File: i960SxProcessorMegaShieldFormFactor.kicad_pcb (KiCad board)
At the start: 4 copper layers, 101.6 x 53.3 mm, 44 parts, among them P1 Power, P2 Data Lines Lower, P3 Data Lines Upper, P4 Address Lines, P5 PWM, P6 Serializable Pins, P7 1284p Direct Connection, U1 74HC245, U2 74HC245, U3 80960Sx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

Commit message: More fix up actions
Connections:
- net /DT\~R renamed /DT\~{R}
- net /Sheet62305775/~MR0 renamed /Sheet62305775/~{MR0}
- net /Sheet62305775/~MR1 renamed /Sheet62305775/~{MR1}
- net /W\~R~ renamed /W\~{R}
- net /~AS renamed /~{AS}
- net /~BE0 renamed /~{BE0}
- net /~BE1 renamed /~{BE1}
- net /~BLAST~\~FAIL~ renamed /~{BLAST}\~{FAIL}
- net /~DEN renamed /~{DEN}
- net /~INT0 renamed /~{INT0}
- net /~INT3 renamed /~{INT3}
- net /~LOCK renamed /~{LOCK}
- net /~READY renamed /~{READY}
- net /~READY960 renamed /~{READY960}
- net /~RESET960 renamed /~{RESET960}
- P1 pad 1: Net-(P1-Pad1) -> unconnected-(P1-Pad1)
- P1 pad 3: Net-(P1-Pad3) -> unconnected-(P1-Pad3)
- P1 pad 8: Net-(P1-Pad8) -> unconnected-(P1-Pad8)
- P5 pad 5: Net-(P5-Pad5) -> unconnected-(P5-Pad5)
- U3 pad 23: Net-(U3-Pad23) -> unconnected-(U3-Pad23)
- U3 pad 42: Net-(U3-Pad42) -> unconnected-(U3-Pad42)
- U3 pad 50: Net-(U3-Pad50) -> unconnected-(U3-Pad50)
- U3 pad 65: Net-(U3-Pad65) -> unconnected-(U3-Pad65)
- U3 pad 75: Net-(U3-Pad75) -> unconnected-(U3-Pad75)
- U7 pad 12: Net-(U7-Pad12) -> unconnected-(U7-Pad12)
- U7 pad 13: Net-(U7-Pad13) -> unconnected-(U7-Pad13)
- U7 pad 14: Net-(U7-Pad14) -> unconnected-(U7-Pad14)
- U7 pad 15: Net-(U7-Pad15) -> unconnected-(U7-Pad15)
- U7 pad 2: Net-(U7-Pad2) -> unconnected-(U7-Pad2)
- U7 pad 3: Net-(U7-Pad3) -> unconnected-(U7-Pad3)
- U7 pad 4: Net-(U7-Pad4) -> unconnected-(U7-Pad4)
- U7 pad 5: Net-(U7-Pad5) -> unconnected-(U7-Pad5)
- U7 pad 6: Net-(U7-Pad6) -> unconnected-(U7-Pad6)
- U7 pad 7: Net-(U7-Pad7) -> unconnected-(U7-Pad7)
- U9 pad 14: Net-(U9-Pad14) -> unconnected-(U9-Pad14)
- U9 pad 15: Net-(U9-Pad15) -> unconnected-(U9-Pad15)
- U9 pad 2: Net-(U9-Pad2) -> unconnected-(U9-Pad2)
- U9 pad 3: Net-(U9-Pad3) -> unconnected-(U9-Pad3)
- U9 pad 4: Net-(U9-Pad4) -> unconnected-(U9-Pad4)
- U9 pad 5: Net-(U9-Pad5) -> unconnected-(U9-Pad5)
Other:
- net class Default removed
- net class Min removed
- board text added: "CLK N\C FAIL GND N\C ~{RDY ALE }AS ~{LOCK }BLAST"
- board text added: "DT\~{R }DEN W\~{R}"
- board text added: "HOLD HLDA ~{INT3 INT2 INT1}"
- board text added: "~{INT0 }RESET960 CLK2 ~{BE0 }BE1 BA1 BA2 BA3"
- board text removed: "CLK N\C FAIL GND N\C ~RDY ALE ~AS ~LOCK ~BLAST"
- board text removed: "DT\~R ~DEN W\~R"
- board text removed: "HOLD HLDA ~INT3 INT2 INT1"
- board text removed: "~INT0 ~RESET960 CLK2 ~BE0 ~BE1 BA1 BA2 BA3"

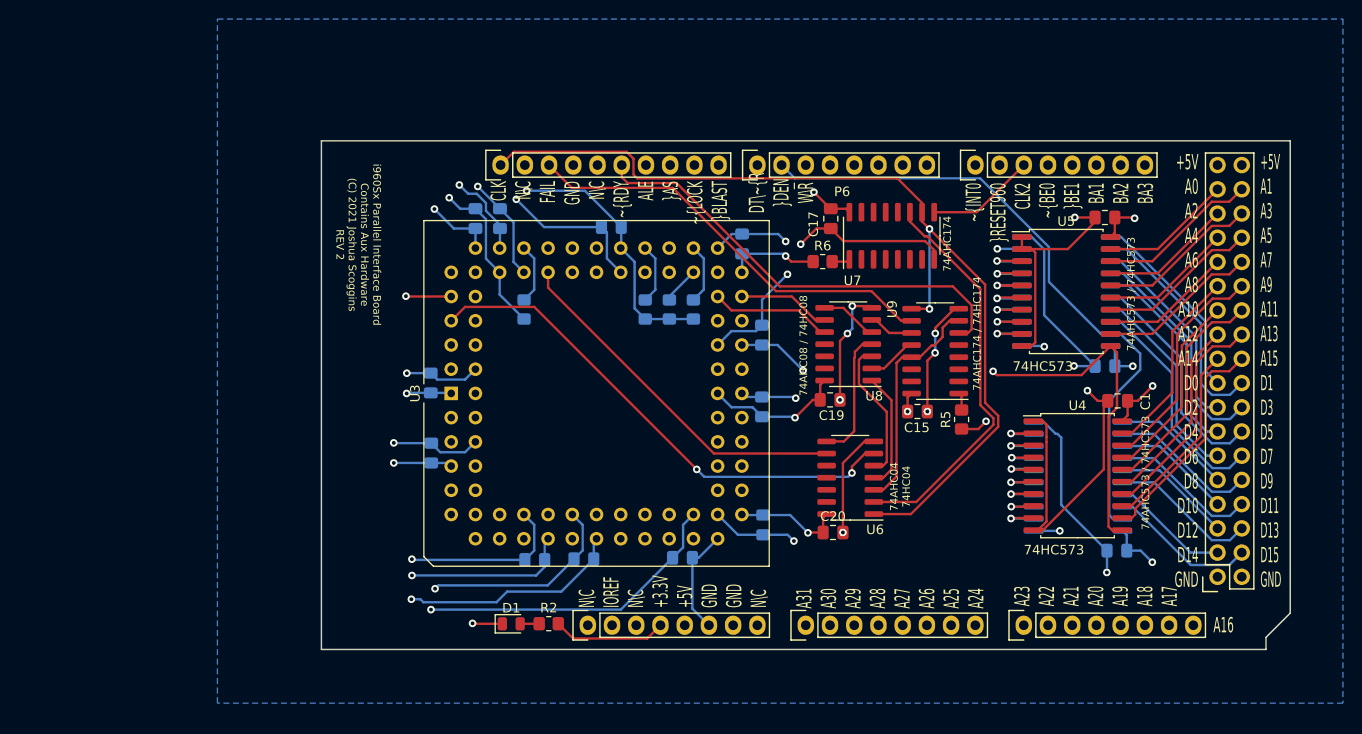
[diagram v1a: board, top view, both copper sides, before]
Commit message: Use a GAL chip to consolidate the number of chips
I have many extra free entries on the GAL to assist me in doing stuff
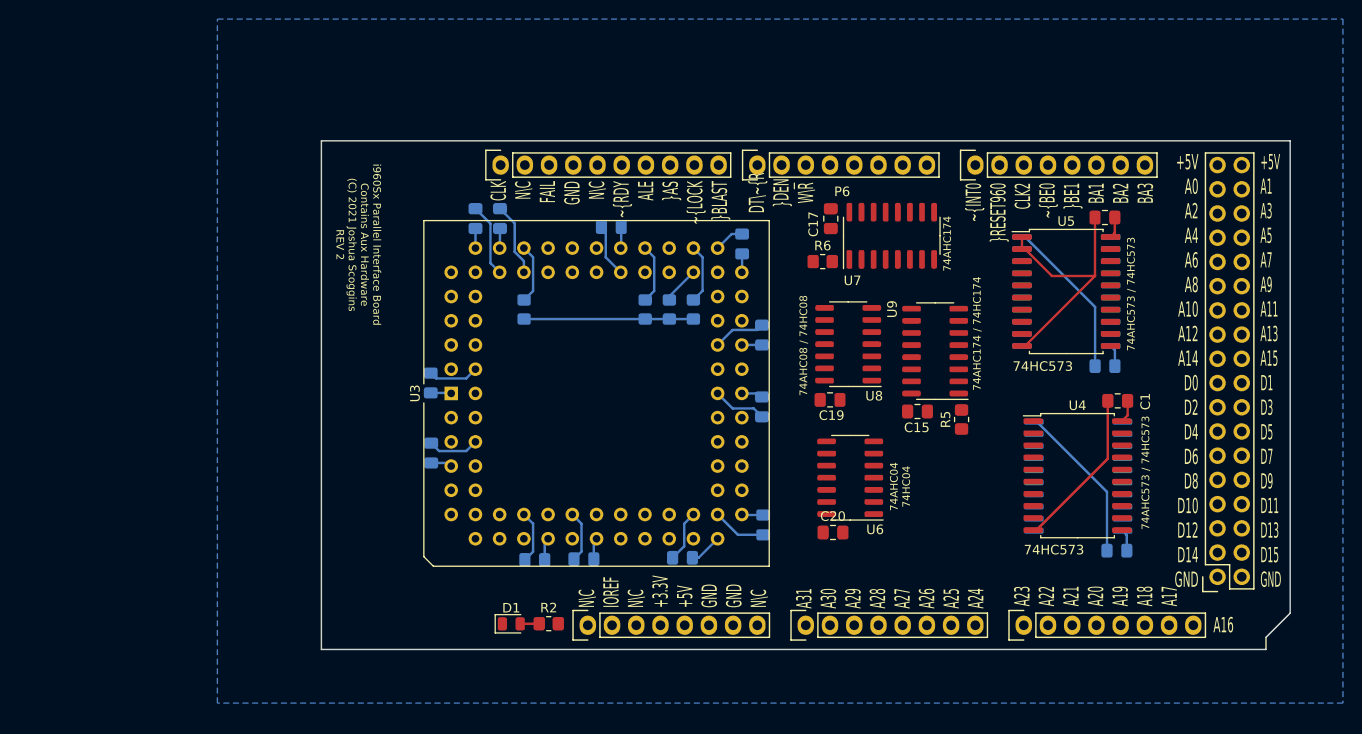
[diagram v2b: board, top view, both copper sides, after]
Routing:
- net GND: track 291.8 -> 119.7 mm, vias 25 -> 0
- net +5V: track 213.9 -> 80.5 mm, vias 19 -> 0
- net /ALE: track 120.5 -> 0.00 mm, vias 1 -> 0
- net /CLK_DIV2: track 101.9 -> 0.00 mm, vias 2 -> 0
- net /DT\~{R}: track 100.8 -> 0.00 mm, vias 2 -> 0
- net /~{DEN}: track 97.7 -> 0.00 mm
- net /A17: track 76.0 -> 0.00 mm
- net /A16: track 74.0 -> 0.00 mm
- net /A19: track 73.4 -> 0.00 mm
- net /A29: track 72.5 -> 0.00 mm
- net /A31: track 71.8 -> 0.00 mm
- net /A18: track 71.4 -> 0.00 mm
- net /A21: track 70.9 -> 0.00 mm
- net /A26: track 69.9 -> 0.00 mm
- net /A28: track 69.6 -> 0.00 mm
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
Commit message: Just do the consolidation
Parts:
- removed U4, U5: 74HC573, Package_SO:SOIC-20W_7.5x12.8mm_P1.27mm
- removed U6: 74AHC04, Package_SO:SOIC-14_3.9x8.7mm_P1.27mm
- removed U9: 74AHC174, Package_SO:SOIC-16_3.9x9.9mm_P1.27mm
- added C21: 0.1uF, Capacitor_SMD:C_0805_2012Metric_Pad1.18x1.45mm_HandSolder, B.Cu at (149.7, 96.1)
- added C22: 0.1uF, Capacitor_SMD:C_0805_2012Metric_Pad1.18x1.45mm_HandSolder, F.Cu at (73.4, 64.3)
- C14, C16: moved to F.Cu
- U1: value 74HC245 -> 74LVC16T245; footprint Package_SO:SOIC-20W_7.5x12.8mm_P1.27mm -> Package_SO:TSSOP-48_6.1x12.5mm_P0.5mm; moved to F.Cu
- U2: value 74HC245 -> 74AHC16373; footprint Package_SO:SOIC-20W_7.5x12.8mm_P1.27mm -> Package_SO:TSSOP-48_6.1x12.5mm_P0.5mm; moved to F.Cu
- U7: value 74AHC174 -> 74AHC74; footprint Package_SO:SOIC-16_3.9x9.9mm_P1.27mm -> Package_SO:SOIC-14_3.9x8.7mm_P1.27mm
- U8: value 74AHC08 -> GAL16V8; footprint Package_SO:SOIC-14_3.9x8.7mm_P1.27mm -> Package_LCC:PLCC-20_THT-Socket
- moved C14 30.0 mm to (189.6, 81.4), turned to 0 degrees
- moved C13 25.6 mm to (173.5, 105.4)
- moved C1 18.6 mm to (173.1, 108.1)
- moved U8 7.40 mm to (166.0, 88.9), turned to 0 degrees
- moved C16 6.40 mm to (189.6, 87.0), turned to 0 degrees
- moved U2 1.13 mm to (182.6, 84.2), turned to 180 degrees
- turned U1 to 180 degrees
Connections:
- C13 pad 1: +5V -> VCC
- C14 pad 1: +5V -> VCC
- C15 pad 1: +5V -> VCC
- C16 pad 1: +5V -> VCC
- C18 pad 1: +5V -> VCC
- C20 pad 1: +5V -> VCC
- P1 pad 2: +5V -> VCC
- R6 pad 2: /Sheet62305775/~{MR1} -> /Sheet62305775/~{SR0}
- U1 pad 11: /D8 -> /D9
- U1 pad 12: /D9 -> /D8
- U1 pad 13: /D10 -> /D7
- U1 pad 14: /D11 -> /D6
- U1 pad 15: /D12 -> GND
- U1 pad 16: /D13 -> /D5
- U1 pad 17: /D14 -> /D4
- U1 pad 18: /D15 -> VCC
- U1 pad 19: /~{DEN} -> /D3
- U1 pad 2: /AD15 -> /D15
- U1 pad 20: +5V -> /D2
- U1 pad 3: /AD14 -> /D14
- U1 pad 4: /AD13 -> GND
- U1 pad 5: /AD12 -> /D13
- U1 pad 6: /AD11 -> /D12
- U1 pad 7: /AD10 -> VCC
- U1 pad 8: /AD9 -> /D11
- U1 pad 9: /AD8 -> /D10
- U2 pad 1: /DT\~{R} -> /HLDA
- U2 pad 11: /D0_OUT -> /A9
- U2 pad 12: /D1 -> /A8
- U2 pad 13: /D2 -> /A7
- U2 pad 14: /D3 -> /A6
- U2 pad 15: /D4 -> GND
- U2 pad 16: /D5 -> /A5
- U2 pad 17: /D6 -> /A4
- U2 pad 18: /D7 -> VCC
- U2 pad 19: /~{DEN} -> /A3
- U2 pad 2: /AD7 -> /A15
- U2 pad 20: +5V -> /A2
- U2 pad 3: /AD6 -> /A14
- U2 pad 4: /AD5 -> GND
- U2 pad 5: /AD4 -> /A13
- U2 pad 6: /AD3 -> /A12
- U2 pad 7: /AD2 -> VCC
- U2 pad 8: /AD1 -> /A11
- U2 pad 9: /D0 -> /A10
- U7 pad 1: /Sheet62305775/~{MR1} -> /Sheet62305775/~{MR0}
- U7 pad 10: /CLK_DIV2 -> (no net)
- U7 pad 11: Net-(U6-Pad2) -> (no net)
- U7 pad 12: unconnected-(U7-Pad12) -> (no net)
- U7 pad 13: unconnected-(U7-Pad13) -> (no net)
- U7 pad 14: unconnected-(U7-Pad14) -> +5V
- U7 pad 2: unconnected-(U7-Pad2) -> Net-(U7-Pad2)
- U7 pad 3: unconnected-(U7-Pad3) -> /CLKO
- U7 pad 4: unconnected-(U7-Pad4) -> /Sheet62305775/~{SR0}
- U7 pad 5: unconnected-(U7-Pad5) -> /CLK_DIV2
- U7 pad 6: unconnected-(U7-Pad6) -> Net-(U7-Pad2)
- U7 pad 7: unconnected-(U7-Pad7) -> GND
- U7 pad 8: GND -> (no net)
- U7 pad 9: /CLKO -> (no net)
- U8 pad 1: Net-(U6-Pad4) -> /CLK_DIV2
- U8 pad 10: /~{BE0} -> GND
- U8 pad 11: (no net) -> unconnected-(U8-Pad11)
- U8 pad 12: (no net) -> unconnected-(U8-Pad12)
- U8 pad 13: (no net) -> unconnected-(U8-Pad13)
- U8 pad 14: +5V -> unconnected-(U8-Pad14)
- U8 pad 2: /Sheet62305775/Z1 -> /~{READY}
- U8 pad 3: Net-(U6-Pad5) -> /Sheet62305775/Z
- U8 pad 4: Net-(U6-Pad8) -> /Sheet62305775/X
- U8 pad 5: Net-(U8-Pad5) -> /~{BE0}
- U8 pad 6: /Sheet62305775/FAIL_SYNC -> /~{BE1}
- U8 pad 7: GND -> /~{BLAST}\~{FAIL}
- U8 pad 8: Net-(U8-Pad5) -> unconnected-(U8-Pad8)
- U8 pad 9: /~{BE1} -> unconnected-(U8-Pad9)
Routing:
- net GND: track 119.7 -> 42.0 mm
- net +5V: track 80.5 -> 71.3 mm

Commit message: Finished retracing
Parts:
- C13: moved to F.Cu
- C19: moved to B.Cu
- moved C22 108.2 mm to (175.3, 100.8), turned to 180 degrees
- moved C20 33.4 mm to (175.3, 81.4), turned to 180 degrees
- moved C15 25.7 mm to (189.7, 106.3)
- moved R5 17.2 mm to (159.4, 84.5)
- moved C13 16.9 mm to (189.7, 100.7), turned to 0 degrees
- moved C18 14.7 mm to (175.4, 87.0)
- moved C19 11.3 mm to (167.6, 92.6)
- moved R6 8.03 mm to (163.2, 84.5), turned to 90 degrees
- moved U8 5.76 mm to (161.7, 92.7)
- moved C1 2.88 mm to (175.3, 106.2)
- moved C17 0.68 mm to (157.5, 76.5)
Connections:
- U2 pad 26: /AD0 -> GND
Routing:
- net VCC: track 0.00 -> 136.8 mm, vias 0 -> 6
- net /AD15: track 0.00 -> 131.1 mm, vias 0 -> 1
- net +5V: track 71.3 -> 200.2 mm, vias 0 -> 14
- net /AD14: track 0.00 -> 122.0 mm, vias 0 -> 1
- net /AD12: track 0.00 -> 116.4 mm, vias 0 -> 1
- net /AD13: track 0.00 -> 112.1 mm, vias 0 -> 1
- net /AD11: track 0.00 -> 111.7 mm, vias 0 -> 1
- net /AD10: track 0.00 -> 111.4 mm, vias 0 -> 1
- net GND: track 42.0 -> 149.7 mm, vias 0 -> 29
- net /AD8: track 0.00 -> 105.5 mm, vias 0 -> 1
- net /DT\~{R}: track 0.00 -> 102.3 mm, vias 0 -> 3
- net /AD9: track 0.00 -> 101.8 mm, vias 0 -> 1
- net /~{DEN}: track 0.00 -> 100.5 mm, vias 0 -> 2
- net /ALE: track 0.00 -> 96.3 mm, vias 0 -> 3
- net /AD7: track 0.00 -> 95.1 mm, vias 0 -> 1
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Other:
- board text added: "CLK N\C FAIL GND N\C ~{RDY} ALE ~{AS} ~{LOCK} ~{BLAST}"
- board text added: "DT\~{R} ~{DEN} W\~{R}"
- board text added: "HOLD HLDA ~{INT3} INT2 INT1"
- board text added: "~{INT0} ~{RESET960} CLK2 ~{BE0} ~{BE1} BA1 BA2 BA3"
- board text removed: "74AHC04 74HC04"
- board text removed: "74AHC08 / 74HC08"
- board text removed: "74AHC174 / 74HC174"
- board text removed: "74AHC573 / 74HC573"
- board text removed: "CLK N\C FAIL GND N\C ~{RDY ALE }AS ~{LOCK }BLAST"
- board text removed: "DT\~{R }DEN W\~{R}"
- board text removed: "HOLD HLDA ~{INT3 INT2 INT1}"
- board text removed: "~{INT0 }RESET960 CLK2 ~{BE0 }BE1 BA1 BA2 BA3"

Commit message: Update tags and add GAL16V8 script
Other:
- board text added: "GAL16V8 Synchronizer CLK S Z X B0 B1 BL NC NC GND NC NC NC NC NC FL X0 Z0 RDY VCC Z0.R = S X0.R = Z /RDY = X * /Z FL.R = B0 * B1 * /BL DESCRIPTION i960 Aux Hardware"
- board text added: "JLCJLCJLCJLC"
- board text added: "Resistor Map R1 - 910 Ohm R2 - [560, 1k] Ohm R3 - 10k R4 - 10k R5 - 10k R6 - 10k R7 - 10k"
- board text added: "i960Sx Parallel Interface Board Contains Aux Hardware (C) 2022 Joshua Scoggins REV 3"
- board text removed: "Resistor Map R1 - 910 Ohm R2 - 560 - 1k Ohm R3 - 10k R4 - 10k R5 - 10k R6 - 10k R7 - 10k"
- board text removed: "i960Sx Parallel Interface Board Contains Aux Hardware (C) 2021 Joshua Scoggins REV 2"
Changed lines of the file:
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@@
   (gr_line (start 204.978 117.856) (end 202.438 120.396) (layer "Edge.Cuts") (width 0.15))
   (gr_line (start 202.438 121.666) (end 103.378 121.666) (layer "Edge.Cuts") (width 0.15))
+  (gr_text "JLCJLCJLCJLC" (at 107.696 106.68 -90) (layer "B.SilkS")
+    (effects (font (size 0.8128 0.8128) (thickness 0.1524)) (justify mirror))
+  )
   (gr_text "HOLD\nHLDA\n~{INT3}\nINT2\nINT1" (at 161.92246 72.48398 90) (layer "B.SilkS")
     (effects (font (size 1.6 0.8) (thickness 0.15)) (justify left mirror))
   )
-  (gr_text "Resistor Map\nR1 - 910 Ohm\nR2 - 560 - 1k Ohm\nR3 - 10k\nR4 - 10k\nR5 - 10k\nR6 - 10k\nR7 - 10k" (at 140.82014 96.91116) (layer "B.SilkS")
-    (effects (font (size 0.8 0.8) (thickness 0.1)) (justify left mirror))
+  (gr_text "GAL16V8\nSynchronizer\n\nCLK S  Z  X  B0 B1 BL NC NC  GND\nNC  NC NC NC NC FL X0 Z0 RDY VCC\n\nZ0.R = S\nX0.R = Z\n/RDY = X * /Z\nFL.R = B0 * B1 * /BL\n\nDESCRIPTION\n\ni960 Aux Hardware\n" (at 131.953 96.52) (layer "B.SilkS")
+    (effects (font (size 0.8128 0.8128) (thickness 0.1524)) (justify mirror))
   )
-  (gr_text "i960Sx Parallel Interface Board\nContains Aux Hardware\n(C) 2021 Joshua Scoggins\nREV 2" (at 107.25658 79.21498 -90) (layer "F.SilkS")
+  (gr_text "i960Sx Parallel Interface Board\nContains Aux Hardware\n(C) 2022 Joshua Scoggins\nREV 3" (at 107.25658 79.21498 -90) (layer "F.SilkS")
     (effects (font (size 0.8 0.8) (thickness 0.1)))
   )
@@
     (effects (font (size 1.6 0.7) (thickness 0.15)) (justify left))
   )
+  (gr_text "Resistor Map\nR1 - 910 Ohm\nR2 - [560, 1k] Ohm\nR3 - 10k\nR4 - 10k\nR5 - 10k\nR6 - 10k\nR7 - 10k" (at 104.394 116.205) (layer "F.SilkS")
+    (effects (font (size 0.8 0.8) (thickness 0.1)) (justify left))
+  )
   (gr_text "A16" (at 197.993 119.12346) (layer "F.SilkS")

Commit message: Finished initial design
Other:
- board text added: "74AHC16373"
- board text added: "74AHC74"
- board text added: "74LVC16T245"
- board text added: "GAL16V8 PLCC20"
- board text removed: "74AHC174"
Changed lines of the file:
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@@
     (property "Sheetname" "")
     (attr smd)
-    (fp_text reference "C6" (at 0 1.68 90) (layer "B.SilkS")
+    (fp_text reference "C6" (at 2.39522 -0.02794 180) (layer "B.SilkS")
       (effects (font (size 1 1) (thickness 0.15)) (justify mirror))
     )
@@
     (property "Sheetname" "")
     (attr smd)
-    (fp_text reference "C7" (at 0 1.68 90) (layer "B.SilkS")
+    (fp_text reference "C7" (at 3.04292 -0.0381 180) (layer "B.SilkS")
       (effects (font (size 1 1) (thickness 0.15)) (justify mirror))
     )
@@
     (property "Sheetname" "Sheet62305775")
     (attr smd)
-    (fp_text reference "C19" (at 0.16002 -1.64084) (layer "B.SilkS")
+    (fp_text reference "C19" (at 1.778 1.905 180) (layer "B.SilkS")
       (effects (font (size 1 1) (thickness 0.15)) (justify mirror))
     )
@@
   (gr_line (start 204.978 117.856) (end 202.438 120.396) (layer "Edge.Cuts") (width 0.15))
   (gr_line (start 202.438 121.666) (end 103.378 121.666) (layer "Edge.Cuts") (width 0.15))
+  (gr_text "74LVC16T245" (at 182.753 103.505 90) (layer "B.SilkS")
+    (effects (font (size 0.8128 0.8128) (thickness 0.1524)) (justify mirror))
+  )
   (gr_text "JLCJLCJLCJLC" (at 107.696 106.68 -90) (layer "B.SilkS")
     (effects (font (size 0.8128 0.8128) (thickness 0.1524)) (justify mirror))
@@
     (effects (font (size 0.8128 0.8128) (thickness 0.1524)) (justify mirror))
   )
+  (gr_text "74AHC16373" (at 182.88 83.947 90) (layer "B.SilkS")
+    (effects (font (size 0.8128 0.8128) (thickness 0.1524)) (justify mirror))
+  )
   (gr_text "i960Sx Parallel Interface Board\nContains Aux Hardware\n(C) 2022 Joshua Scoggins\nREV 3" (at 107.25658 79.21498 -90) (layer "F.SilkS")
     (effects (font (size 0.8 0.8) (thickness 0.1)))
@@
     (effects (font (size 1.6 0.8) (thickness 0.1)))
   )
+  (gr_text "GAL16V8 PLCC20" (at 161.544 106.807) (layer "F.SilkS")
+    (effects (font (size 0.8128 0.8128) (thickness 0.1524)))
+  )
   (gr_text "A23\nA22\nA21\nA20\nA19\nA18\nA17" (at 184.62244 114.9985 90) (layer "F.SilkS")
     (effects (font (size 1.6 0.8) (thickness 0.15)) (justify right))
@@
     (effects (font (size 1.6 0.8) (thickness 0.15)))
   )
-  (gr_text "74AHC174" (at 169.0243 79.11846 90) (layer "F.SilkS")
+  (gr_text "74AHC74" (at 168.402 78.486 90) (layer "F.SilkS")
     (effects (font (size 0.8 0.8) (thickness 0.1)))
   )
